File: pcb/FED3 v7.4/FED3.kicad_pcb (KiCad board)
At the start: 4 copper layers, 108 x 50 mm, 91 parts, among them IC1 MC74VHC1GT125, IC2 TB6612FNG, IC4 RTC PCF8523T, J1 Conn_02x03_Odd_Even, Q2 DMP2035U-7, SW1 Sw, SW2 SPST_TACT-KMR2, U1 ATSAMD21G18A, U2 MIC5504-3.3, U3 MCP73831T, X1 ClockXtal, X2 uXtal, X4 microsd, X5 JST-XH-02

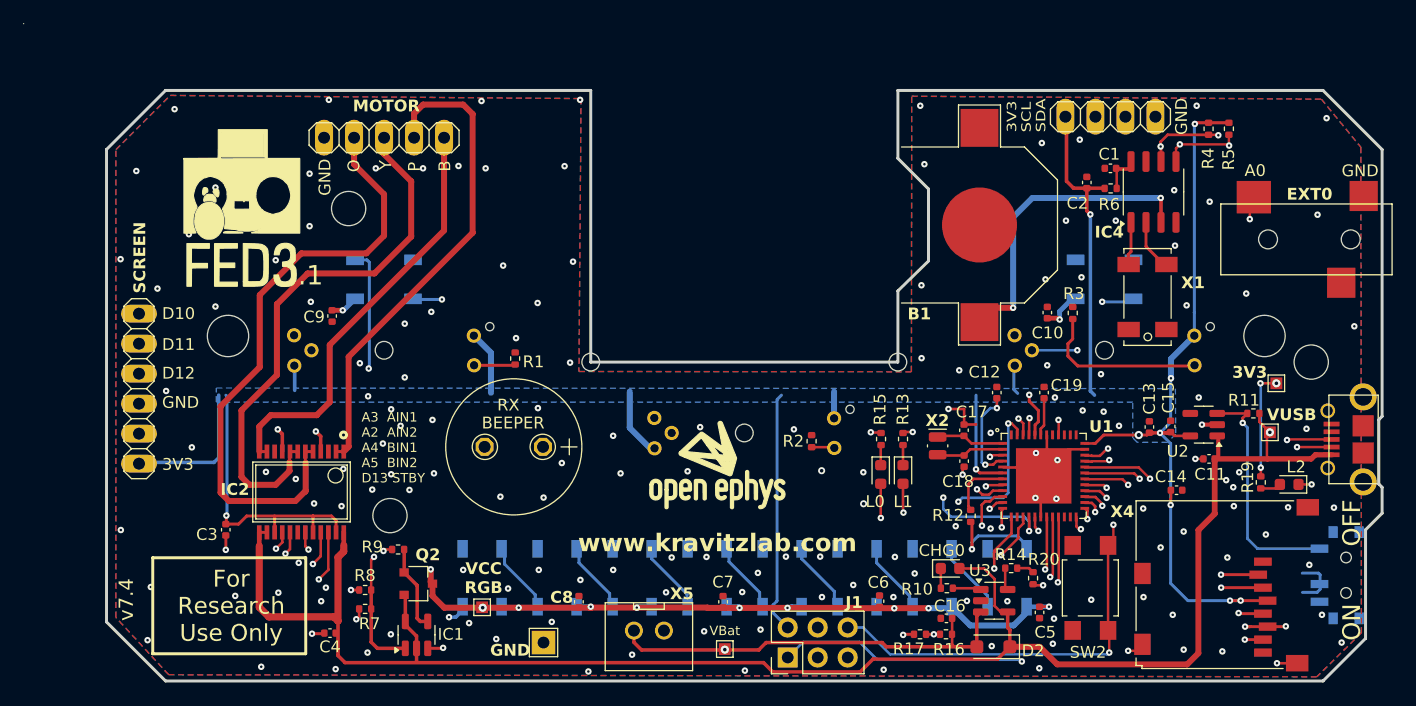
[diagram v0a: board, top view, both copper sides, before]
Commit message: v.7.4 - alterações rail power
v.7.4
- modificada estrutura rail power: VUSB apenas para Vcharging
- modificadas Rs de LEDs para diminuir I
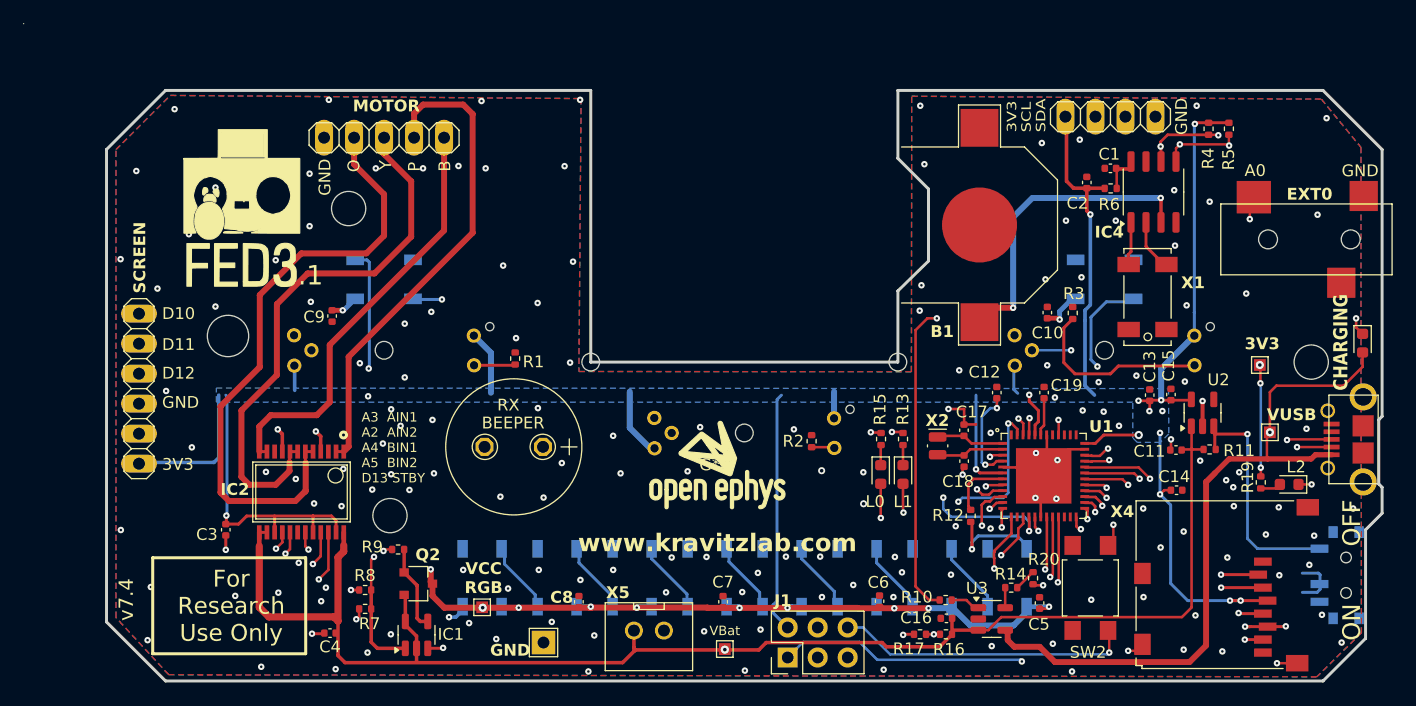
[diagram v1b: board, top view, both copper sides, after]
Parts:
- removed @HOLE4: , 
- removed D2: SM5817PL, Diode_SMD:D_SOD-123F
- G***: footprint FED3.1 v7.4:oe logo -> FED3_PCBLib:oe logo
- L2: value RED -> DNP
- R13: value 68R -> 2k2
- R15: value 68R -> 5k1 10k
- R19: value 68R -> DNP
- moved CHG0 39.8 mm to (200.8, 101.4), turned to -90 degrees
- moved R11 4.80 mm to (187.9, 110.4), turned to 0 degrees
- moved C11 2.90 mm to (185.1, 110.5)
- moved C13 2.70 mm to (182.8, 105.8)
- moved C15 2.70 mm to (184.6, 105.8)
- moved TP1 2.09 mm to (192.2, 103.2)
- moved R14 1.65 mm to (171.1, 122.1)
- moved U3 1.56 mm to (169.4, 124.8)
- moved R10 1.00 mm to (165.6, 123.2)
- moved U2 1.00 mm to (187.3, 107.3), turned to 90 degrees
- moved C5 0.80 mm to (173.5, 123.4), turned to 90 degrees
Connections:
- net D7 renamed /controler stage/D7
- C11 pad 1: VUSB -> VBat
- C4 pad 1: VUSB -> VBat
- IC1 pad 2: VUSB -> VBat
- IC1 pad 5: VUSB -> VBat
- IC2 pad 13: VUSB -> VBat
- IC2 pad 14: VUSB -> VBat
- IC2 pad 24: VUSB -> VBat
- Q2 pad P$2: VUSB -> VBat
- R11 pad 1: VUSB -> VBat
- U2 pad 1: VUSB -> VBat
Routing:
- net VUSB: track 149.2 -> 60.3 mm
- net VBat: track 37.5 -> 125.3 mm
- net Net-(CHG0-K): track 1.67 -> 64.1 mm, vias 0 -> 2
- net /controler stage/~{RESET}: track 48.7 -> 52.4 mm
- net Net-(PI1-Pad2): track 14.3 -> 15.7 mm
- net GND: track 37.2 -> 38.5 mm, vias 157 -> 158
- net +3V3: vias 18 -> 21
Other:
- board text added: "CHARGING"

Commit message: v.7.4 - commit to final review
- I2C plug moved to board front side
- Rs to LEDs changed - impose less I
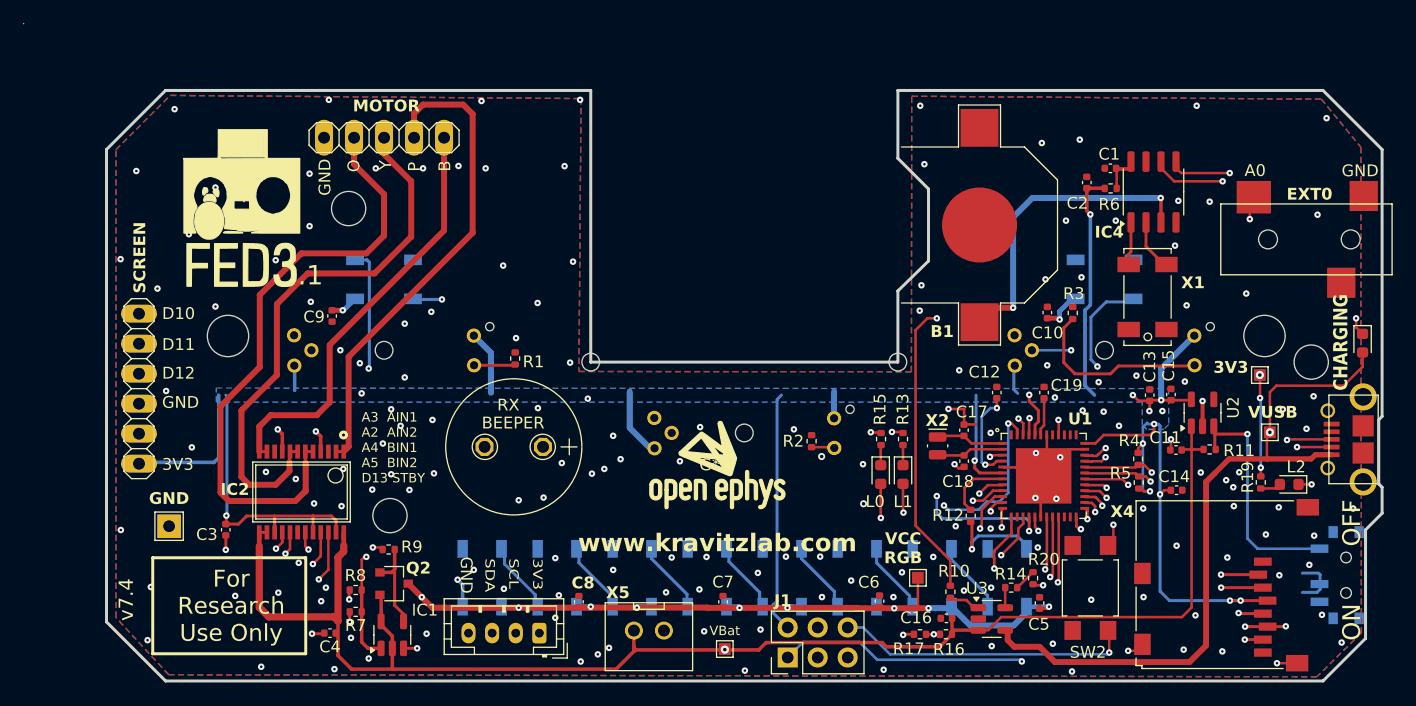
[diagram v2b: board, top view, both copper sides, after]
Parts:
- added ?: , , F.Cu at (212.6, 100.5)
- AUX_I2C0: footprint FED3_PCBLib:1X04 -> Connector_JST:JST_PH_B4B-PH-K_1x04_P2.00mm_Vertical
- R15: value 5k1 10k -> 10k
- moved AUX_I2C0 65.2 mm to (131.2, 126.0), turned to 180 degrees
- moved TP2 37.0 mm to (163.2, 121.3)
- moved TP5 33.2 mm to (99.8, 116.9)
- moved R5 30.9 mm to (181.9, 113.2), turned to -90 degrees
- moved R4 28.6 mm to (181.8, 111.2)
- moved Q2 2.05 mm to (118.8, 121.8)
- moved IC1 2.05 mm to (118.7, 126.1)
- moved TP1 0.85 mm to (192.2, 104.1)
- moved R7 0.84 mm to (115.6, 124.2)
- moved R10 0.81 mm to (165.9, 122.5), turned to -90 degrees
- moved R8 0.80 mm to (115.6, 122.3)
- moved R9 0.80 mm to (118.4, 118.9)
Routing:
- net /controler stage/SDA: track 54.1 -> 117.7 mm, vias 4 -> 5
- net /controler stage/SCL: track 55.4 -> 114.9 mm, vias 4 -> 5
- net +3V3: track 228.6 -> 236.0 mm, vias 21 -> 22
- net /IOs Interface/VCCNEO: track 125.1 -> 130.7 mm, vias 12 -> 11
- net Net-(LED8-DO): track 31.0 -> 29.5 mm
- net A2: track 68.8 -> 70.2 mm
- net Net-(CHG0-K): track 64.1 -> 62.8 mm
- net D13: track 85.2 -> 84.0 mm
- net VBat: track 125.3 -> 126.3 mm
- net Net-(IC1-P$4): track 7.29 -> 7.91 mm
- net /controler stage/D10: track 96.4 -> 97.0 mm
- net GND: vias 158 -> 160

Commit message: FED3 v7.3 - 2nd revision
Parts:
- AUX_I2C0: value DNP -> TBD; footprint Connector_JST:JST_PH_B4B-PH-K_1x04_P2.00mm_Vertical -> Connector_JST:JST_SH_BM04B-SRSS-TB_1x04-1MP_P1.00mm_Vertical
- R11, R16, R17: value 100k -> 100k 0.1%
- moved AUX_I2C0 3.17 mm to (128.0, 126.3)
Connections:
- AUX_I2C0 pad 1: +3V3 -> GND
- AUX_I2C0 pad 2: /controler stage/SCL -> +3V3
- AUX_I2C0 pad 4: GND -> /controler stage/SCL
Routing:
- net +3V3: track 236.0 -> 240.3 mm, vias 22 -> 23
- net /controler stage/SCL: track 114.9 -> 118.1 mm, vias 5 -> 6
- net GND: track 38.5 -> 40.3 mm
- net /controler stage/SDA: track 117.7 -> 119.3 mm, vias 5 -> 6
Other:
- board text added: "Qwiic"
- board text added: "STEMMA QT"

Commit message: modificados valores R14 R20: 2k2
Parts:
- R14, R20: value 1k -> 2k2
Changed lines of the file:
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@@
 			)
 		)
-		(property "Value" "1k"
+		(property "Value" "2k2"
 			(at 0 1.17 0)
 			(layer "F.Fab")
@@
 			)
 		)
-		(property "Description" "SMD 0402 1kΩ ±1% 0.100W"
+		(property "Description" "SMD 0402 2.2kΩ ±1% 0.100W"
 			(at 0 0 180)
 			(unlocked yes)
@@
 			)
 		)
-		(property "OEPSPN" "OEPS020006"
+		(property "OEPSPN" "OEPS020174"
 			(at 0 0 180)
 			(unlocked yes)
@@
 			)
 		)
-		(property "MPN" "ERJ-2RKF1001X"
+		(property "MPN" "ERJ-2RKF2201X"
 			(at 0 0 180)
 			(unlocked yes)
@@
 			)
 		)
-		(property "Value" "1k"
+		(property "Value" "2k2"
 			(at 0 1.17 90)
 			(unlocked yes)
@@
 			)
 		)
-		(property "Description" "SMD 0402 1kΩ ±1% 0.100W"
+		(property "Description" "SMD 0402 2.2kΩ ±1% 0.100W"
 			(at 0 0 90)
 			(unlocked yes)
@@
 			)
 		)
-		(property "OEPSPN" "OEPS020006"
+		(property "OEPSPN" "OEPS020174"
 			(at 0 0 90)
 			(unlocked yes)
@@
 			)
 		)
-		(property "MPN" "ERJ-2RKF1001X"
+		(property "MPN" "ERJ-2RKF2201X"
 			(at 0 0 90)
 			(unlocked yes)

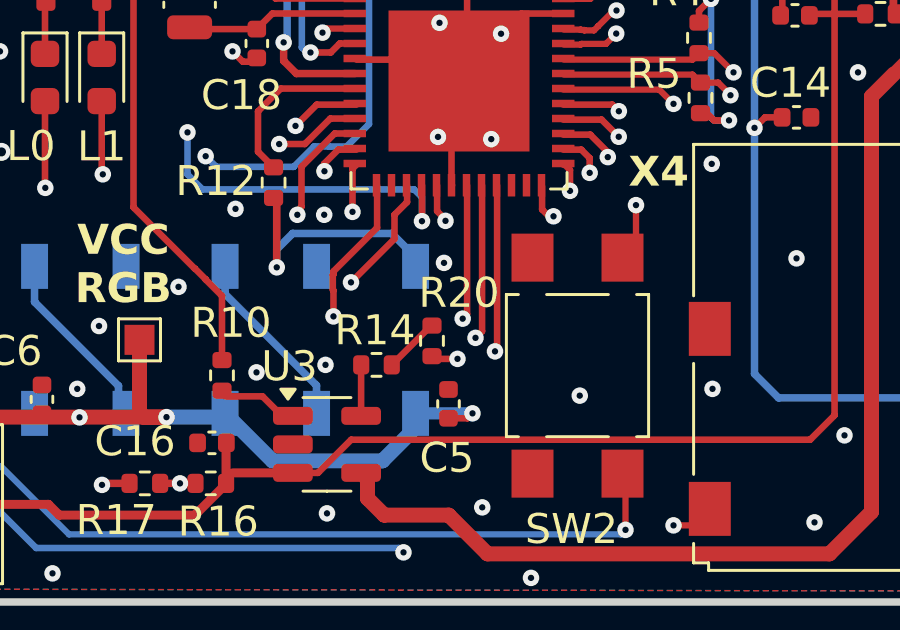
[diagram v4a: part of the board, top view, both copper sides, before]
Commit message: R20 off; R14=2k2
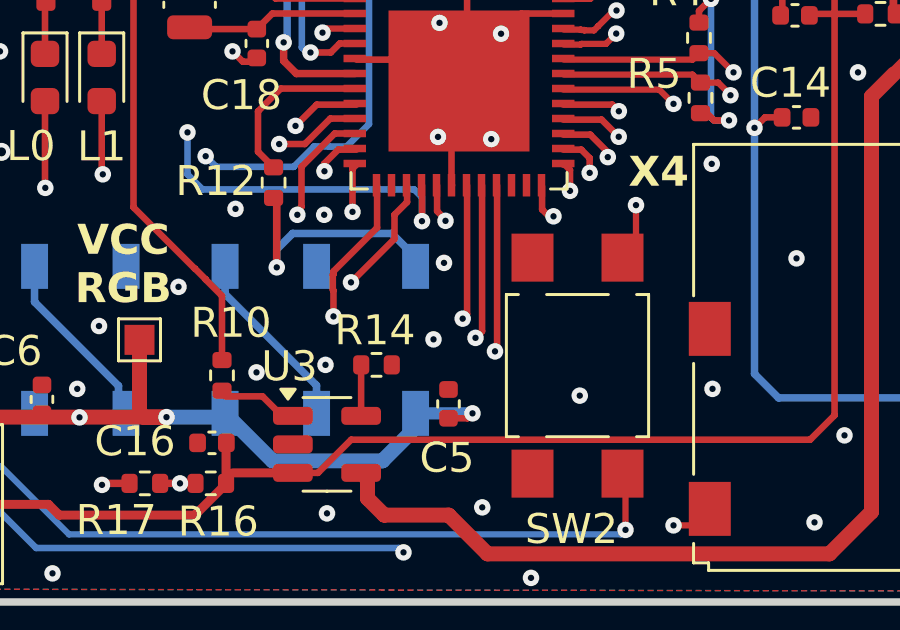
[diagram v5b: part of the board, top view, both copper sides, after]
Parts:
- removed R20: 2k2, Resistor_SMD:R_0402_1005Metric
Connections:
- R14 pad 1: Net-(R14-Pad1) -> GND
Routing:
- net Net-(R14-Pad1): track 1.88 -> 0.00 mm
- net GND: track 40.3 -> 39.6 mm
